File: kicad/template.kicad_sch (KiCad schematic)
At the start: 7 parts, among them J1 Bus_PCI_Express_x1, J6 USB_C_Receptacle_USB2.0_16P, U1 MCP25625T-E/ML, U2 RP2040, U4 W25Q128JVP, X1 ABM8-272-T3, Y1 X322516MLB4SI

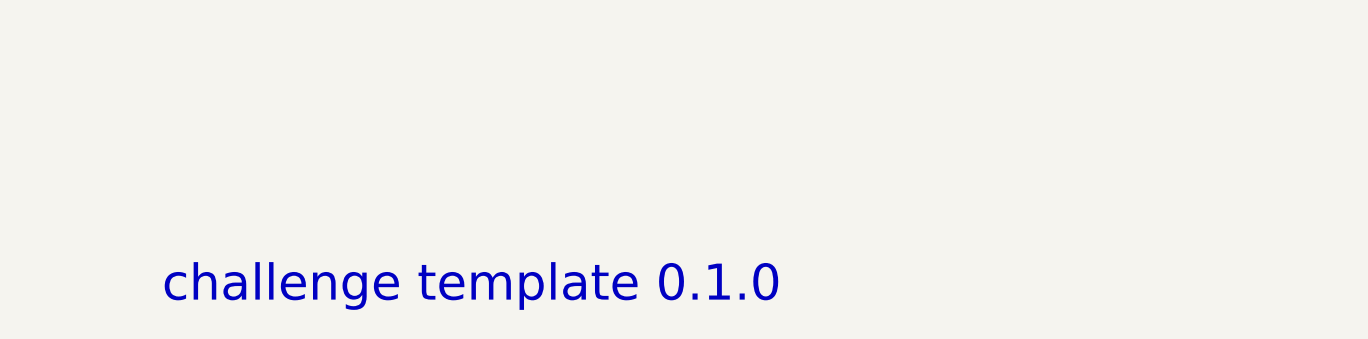
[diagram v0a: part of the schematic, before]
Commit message: init status module
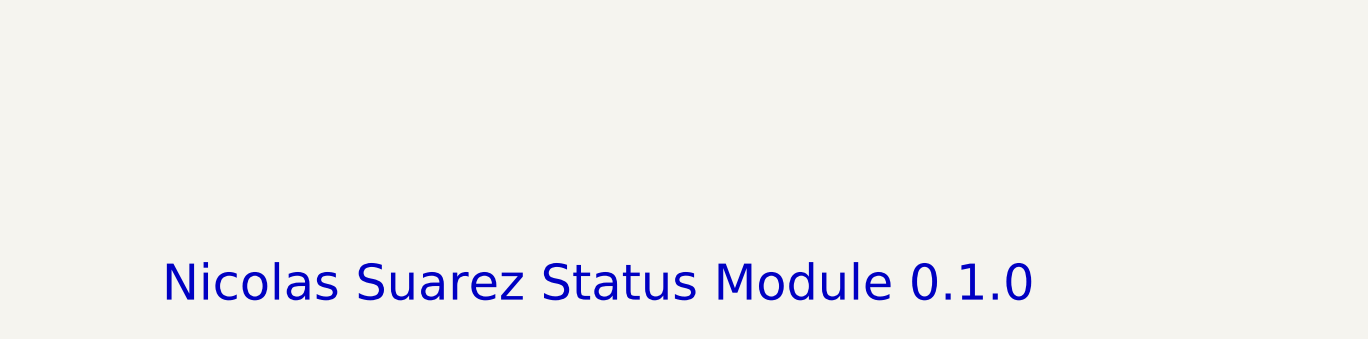
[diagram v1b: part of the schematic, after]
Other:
- note added: "Nicolas Suarez Status Module 0.1.0"
- note removed: "challenge template 0.1.0"
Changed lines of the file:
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@@
 		)
 	)
-	(text "challenge template 0.1.0"
+	(text "Nicolas Suarez Status Module 0.1.0"
 		(exclude_from_sim no)
 		(at 493.014 386.842 0)

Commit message: Update schematic
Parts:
- added C1, C2, C3: 0.1 uF, Capacitor_SMD:C_0603_1608Metric, symbol Device:C
- added C16, C21, C22, C23, C24, C25, C26, C27, C7, C8: 100 nF, Capacitor_SMD:C_0603_1608Metric, symbol Device:C
- added C17, C18: 15 pF, Capacitor_SMD:C_0603_1608Metric, symbol Device:C
- added C19, C20: 10 uF, Capacitor_SMD:C_0603_1608Metric, symbol Device:C
- added C4, C5: 0.22 uF, Capacitor_SMD:C_0603_1608Metric, symbol Device:C
- added C6: 1 uF, Capacitor_SMD:C_0603_1608Metric_Pad1.08x0.95mm_HandSolder, symbol Device:C
- added C9: 1 uF, Capacitor_SMD:C_0603_1608Metric, symbol Device:C
- added J2: Micro_SD_Card, Connector_Card:microSD_HC_Wuerth_693072010801, symbol Connector:Micro_SD_Card
- added J3: Conn_01x02_Pin, Connector_Hirose:Hirose_DF13-02P-1.25DSA_1x02_P1.25mm_Vertical, symbol Connector:Conn_01x02_Pin
- added R3, R6: 1k, Resistor_SMD:R_0603_1608Metric, symbol Device:R
- added R4, R5: 27, Resistor_SMD:R_0603_1608Metric, symbol Device:R
- added R7: DNF, Resistor_SMD:R_0603_1608Metric, symbol Device:R
- added U3: NCP1117-1.5_SOT223, Package_TO_SOT_SMD:SOT-223-3_TabPin2, symbol Regulator_Linear:NCP1117-1.5_SOT223
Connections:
- net +3.3V: now also U1.11 (VIO), U1.3 (VDD), U2.1 (IOVDD), U2.10 (IOVDD), U2.22 (IOVDD), U2.33 (IOVDD), U2.42 (IOVDD), U2.43 (ADC_AVDD), U2.44 (VREG_IN), U2.48 (USB_VDD), U2.49 (IOVDD), U4.8 (VCC), C1.1, C16.2, C2.1, C20.2, C21.2, C22.2, C23.2, C24.2, C25.2, C26.2, C27.2, C9.2, J2.4 (VDD), R7.1, U3.2 (VO)
- net +5V: now also U1.19 (VDDA), C3.2
- net CANN: now also U1.12 (CANL)
- net CANP: now also U1.13 (CANH)
- net GND: now also U1.18 (VSS), U1.22 (GND), U2.19 (TESTEN), U2.57 (GND), U4.4 (GND), X1.2, X1.4, Y1.2, Y1.4, C1.2, C16.1, C17.2, C18.2, C19.1, C2.2, C21.1, C22.1, C23.1, C24.1, C25.1, C26.1, C27.1, C3.1, C4.1, C5.1, C6.1, C7.1, C8.1, C9.1, J2.6 (VSS), J3.2 (Pin_2), U3.1 (GND)
- net CS: now reaches U1.1 (*CS)
- net CS: now also U2.28 (GPIO17)
- net RX: now reaches U1.10 (RXD)
- net RX: now also U1.5 (RXCAN)
- net STBY: now reaches U1.15 (STBY)
- net STBY: now also U2.2 (GPIO0)
- net TX: now reaches U1.16 (TXD)
- net TX: now also U1.4 (TXCAN)
- net RESET: now reaches U1.2 (*RESET)
- net RESET: now also U2.9 (GPIO7)
- net OSC2: now reaches U1.20 (OSC2)
- net OSC2: now also Y1.3, C4.2
- net OSC1: now reaches U1.21 (OSC1)
- net OSC1: now also Y1.1, C5.2
- net SCK: now reaches U1.26 (SCK)
- net SCK: now also U2.29 (GPIO18), J2.5 (CLK)
- net MOSI: now reaches U1.27 (SI)
- net MOSI: now also U2.5 (GPIO3), J2.3 (CMD)
- net MISO: now reaches U1.28 (SO)
- net MISO: now also U2.6 (GPIO4), J2.7 (DAT0)
- net QSPI_SS: now reaches U4.1 (~{CS})
- net QSPI_SS: now also U2.56 (QSPI_SS), R6.1, R7.2
- net QSPI_SD1: now reaches U4.2 (DO(IO1))
- net QSPI_SD1: now also U2.55 (QSPI_SD1)
- net QSPI_SD2: now reaches U4.3 (IO2)
- net QSPI_SD2: now also U2.54 (QSPI_SD2)
- net QSPI_SD0: now reaches U4.5 (DI(IO0))
- net QSPI_SD0: now also U2.53 (QSPI_SD0)
- net QSPI_CLK: now reaches U4.6 (CLK)
- net QSPI_CLK: now also U2.52 (QSPI_SCLK)
- net QSPI_SD3: now reaches U4.7 (IO3)
- net QSPI_SD3: now also U2.51 (QSPI_SD3)
- net CS_SD: now reaches U2.16 (GPIO13)
- net CS_SD: now also J2.2 (DAT3/CD)
- net X_IN: now reaches U2.20 (XIN)
- net X_IN: now also X1.1, C17.1
- net X_OUT: now reaches U2.21 (XOUT)
- net X_OUT: now also R3.1
- net +1V1: now reaches U2.23 (DVDD), U2.50 (DVDD)
- net +1V1: now also U2.45 (VREG_VOUT), C6.2, C7.2, C8.2
- net at U2.46 (USB_DM): now also R5.1
- net at U2.47 (USB_DP): now also R4.1
- net VBUS: now reaches J6.A4 (VBUS), J6.A9 (VBUS), J6.B4 (VBUS), J6.B9 (VBUS)
- net VBUS: now also C19.2, U3.3 (VI)
- net USB_P: now reaches J6.A6 (D+), J6.B6 (D+)
- net USB_P: now also R4.2
- net USB_D: now reaches J6.A7 (D-), J6.B7 (D-)
- net USB_D: now also R5.2
- net at X1.3: now also C18.1, R3.2
- new net: J3.1 (Pin_1), R6.2
- no-connect marks 8 -> 9
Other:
- moved on the sheet: U4, Y1

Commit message: update schematic and pcb layout
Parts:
- removed C20: 10 uF, Capacitor_SMD:C_0603_1608Metric, symbol Device:C
- removed U3: NCP1117-1.5_SOT223, Package_TO_SOT_SMD:SOT-223-3_TabPin2, symbol Regulator_Linear:NCP1117-1.5_SOT223

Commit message: update BOM
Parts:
- removed R7: DNF, Resistor_SMD:R_0603_1608Metric, symbol Device:R
- C1, C2, C3: JLC Link (none) -> https://jlcpcb.com/partdetail/1942-CL10B104KA8NNNC/C1590; LCSC Part # (none) -> C1590
- C16, C21, C22, C23, C24, C25, C26, C27, C7, C8: JLC Link (none) -> https://jlcpcb.com/partdetail/TORCH-CT41G_0603_2X1_50V_0_1_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; LCSC Part # (none) -> C125205
- C17, C18: JLC Link (none) -> https://jlcpcb.com/partdetail/Yageo-CC0603JRNPO9BN150/C1070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; LCSC Part # (none) -> C107037
- C19: JLC Link (none) -> https://jlcpcb.com/partdetail/2043-CL10A106MQ8NNNC/C1691; LCSC Part # (none) -> C1691
- C4, C5: JLC Link (none) -> https://jlcpcb.com/partdetail/1958-0603B224K250NT/C1606; LCSC Part # (none) -> C1606
- C6: footprint Capacitor_SMD:C_0603_1608Metric_Pad1.08x0.95mm_HandSolder -> Capacitor_SMD:C_0603_1608Metric; JLC Link (none) -> https://jlcpcb.com/partdetail/1944-CL10A105KO8NNNC/C1592; LCSC Part # (none) -> C1592
- C9: JLC Link (none) -> https://jlcpcb.com/partdetail/1944-CL10A105KO8NNNC/C1592; LCSC Part # (none) -> C1592
- J2: JLC Link (none) -> https://jlcpcb.com/partdetail/Korean_HropartsElec-TF01A/C91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; LCSC Part # (none) -> C91145
- J3: JLC Link (none) -> https://jlcpcb.com/partdetail/Made_inChina-2_54mm_12P/C36717; LCSC Part # (none) -> C36717
- R3, R6: JLC Link (none) -> https://jlcpcb.com/partdetail/Vo-0603_5_1K/C2889391; LCSC Part # (none) -> C2889391
- R4, R5: JLC Link (none) -> https://jlcpcb.com/partdetail/25933-0603WAF270JT5E/C25190; LCSC Part # (none) -> C25190
- U1: JLC Link (none) -> https://jlcpcb.com/partdetail/MicrochipTech-MCP25625T_EML/C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; LCSC Part # (none) -> C191253
- X1: JLC Link (none) -> https://jlcpcb.com/partdetail/AbraconLlc-ABM8_272T3/C206257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; LCSC Part # (none) -> C20625731
- Y1: JLC Link (none) -> https://jlcpcb.com/partdetail/YangxingTech-X322516MLB4SI/C1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; LCSC Part # (none) -> C13738
